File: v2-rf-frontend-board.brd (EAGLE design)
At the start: 110.3 x 41.6 mm, 63 parts, among them U1 MAX2769, X3 BU-SMA-H

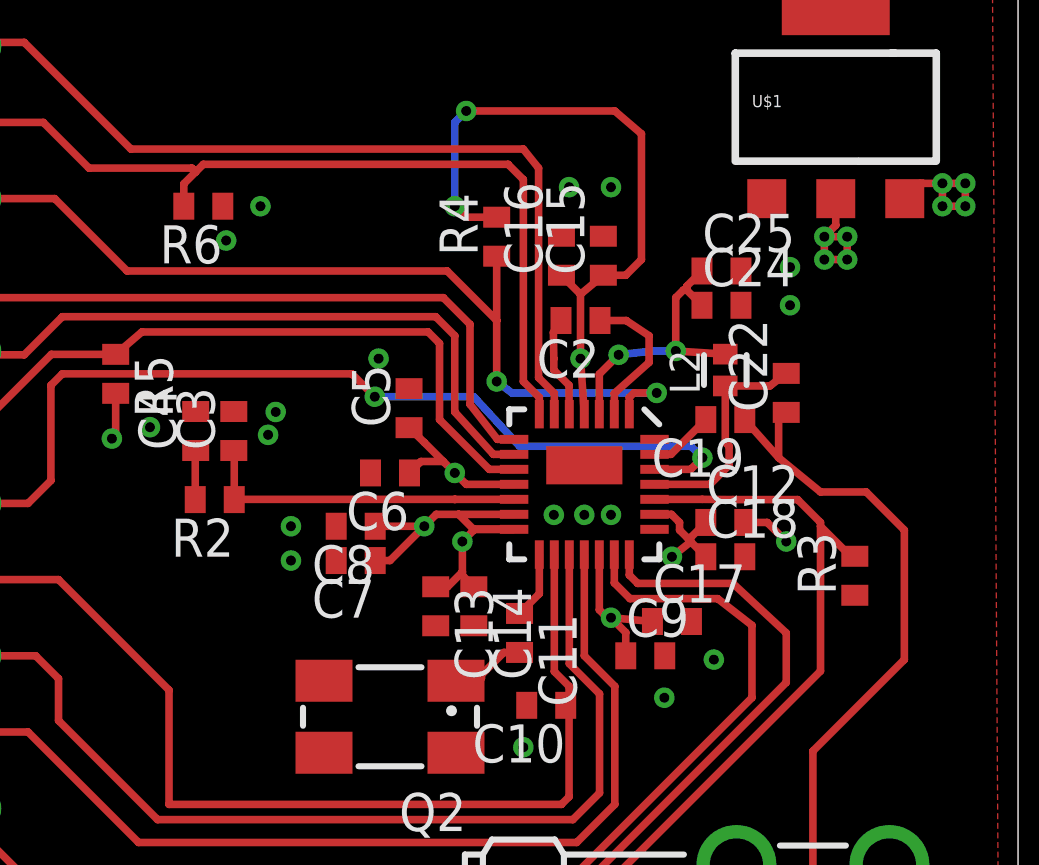
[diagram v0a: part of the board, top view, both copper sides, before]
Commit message: Changed MAX2769 symbol and fixed circuit.
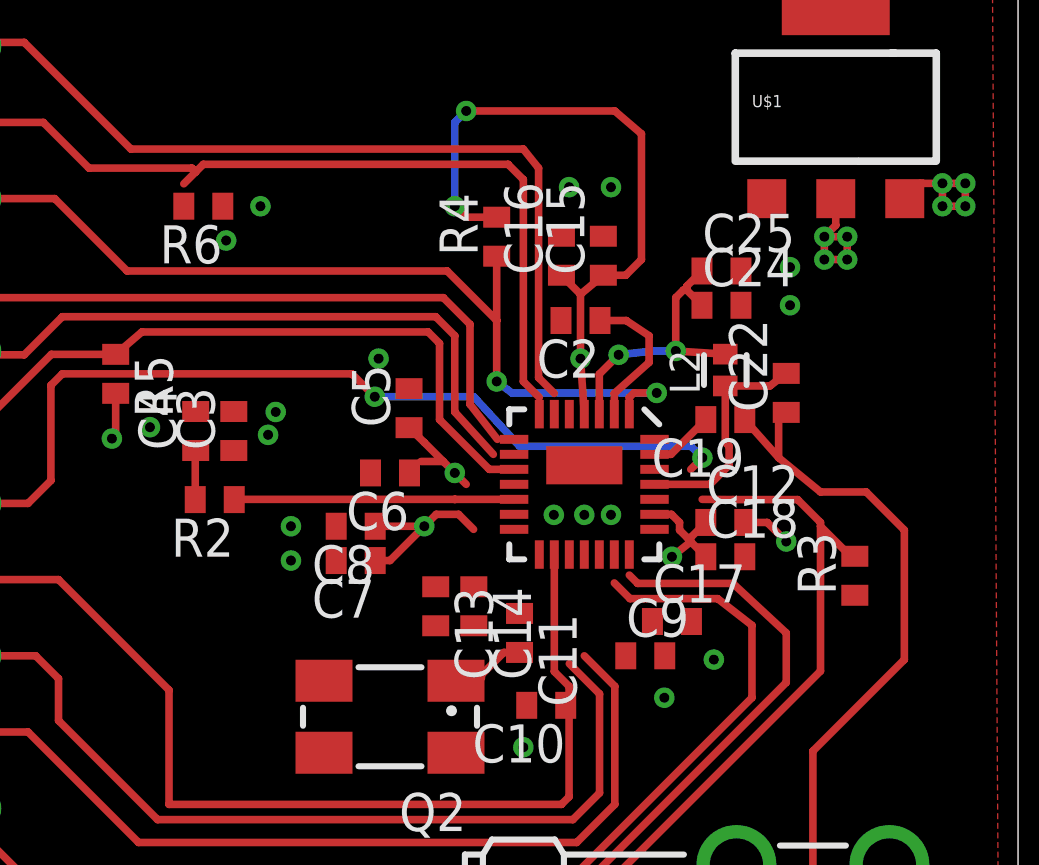
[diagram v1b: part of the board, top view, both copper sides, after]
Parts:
- C11: value 10nF -> 23pF
- Q2: value (none) -> 16.368MHz
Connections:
- net N$35 renamed CPOUT
- net N$41 renamed LNAOUT
- new net N$11: R3.2, U1.24
- new net N$12: U1.26
- new net N$8: R6.1, U1.7
- net 3.3VD: now also C17.2, C9.2; no longer C17.1, C9.1
- net BAR_GND: now also C17.1, C9.1, R6.2; no longer C17.2, C9.2, R6.1
- net IDLE: no longer R3.2, U1.24
- net PGM: no longer U1.26
- net SHDN: no longer R6.2, U1.7
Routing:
- net 3.3VA: track 50.3 -> 40.3 mm, vias 11 -> 10
- net 3.3VD: track 46.7 -> 41.5 mm, vias 23 -> 22
- net Q1: track 87.6 -> 84.0 mm
- net N$13: track 3.41 -> 0.00 mm
- net Q0: track 91.3 -> 88.0 mm
- net N$21: track 2.24 -> 0.00 mm
- net IDLE: track 108.4 -> 106.6 mm
- net CPOUT: track 11.0 -> 9.35 mm
- net SHDN: track 93.3 -> 92.0 mm
- net PGM: track 78.8 -> 77.6 mm
- net I0: track 97.1 -> 96.1 mm
- net N$3: track 2.54 -> 1.69 mm
- net SPI_CLK: track 75.7 -> 75.0 mm
- net LD: track 96.9 -> 96.3 mm
- net I1: track 72.6 -> 71.9 mm
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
